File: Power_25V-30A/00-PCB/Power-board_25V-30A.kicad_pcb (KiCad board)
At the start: 2 copper layers, 14 parts, among them Q1 IRL7486, Q2 IRL7486, U1 AD8418, U2 UCC27210

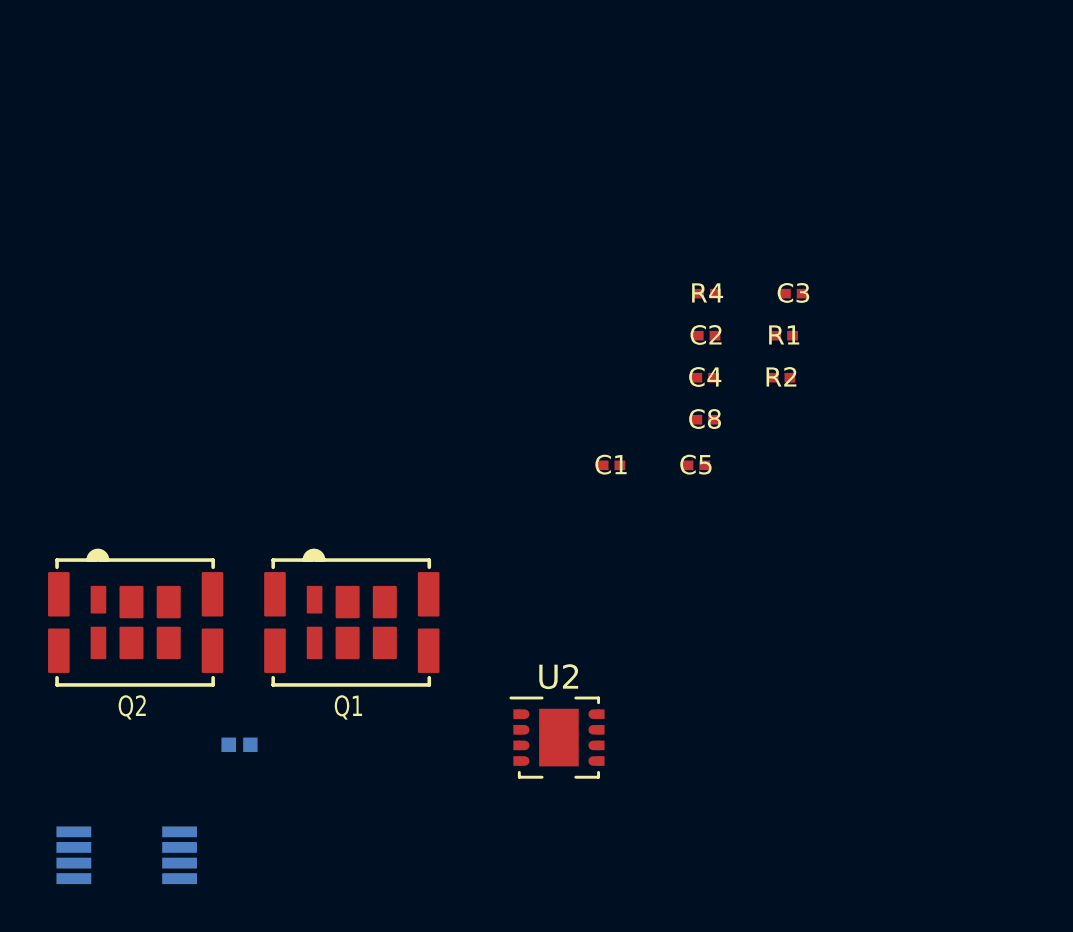
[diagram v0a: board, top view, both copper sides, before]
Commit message: Multiplied Phase Schematics
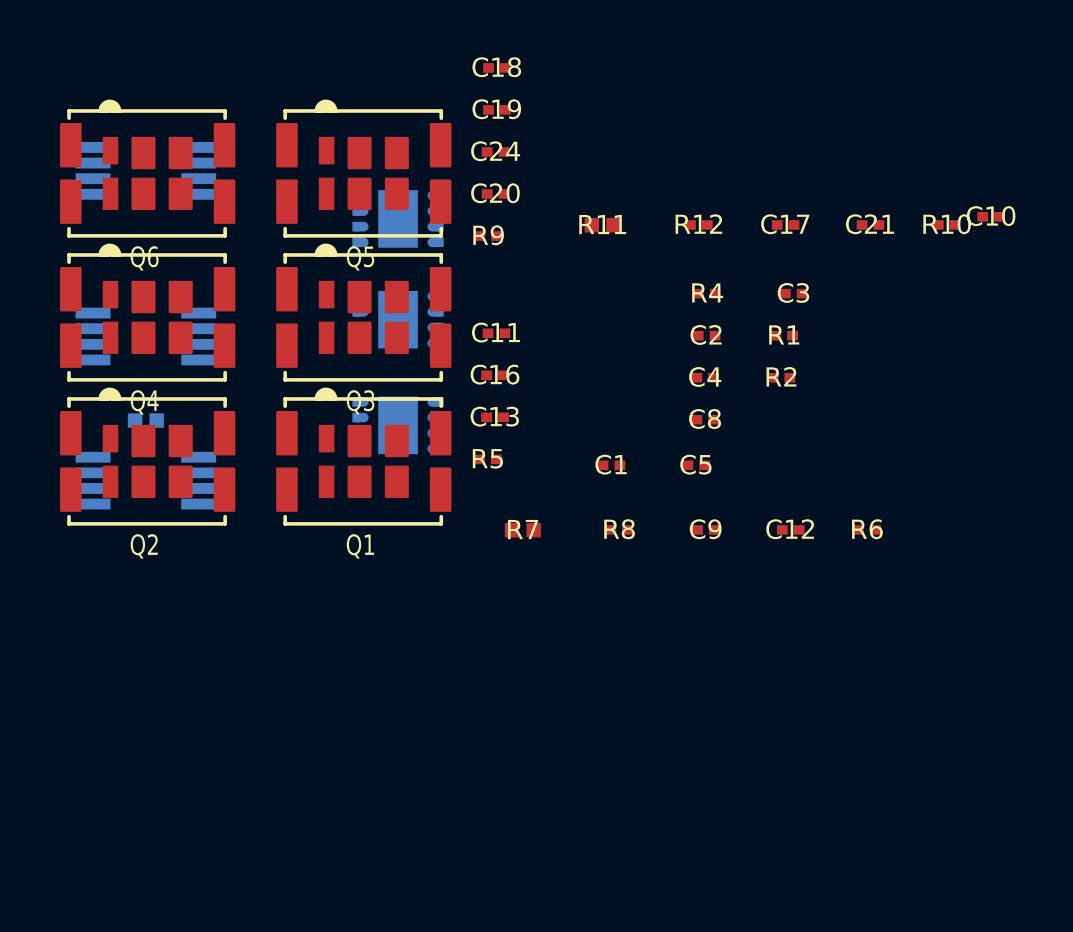
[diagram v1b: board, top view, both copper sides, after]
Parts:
- added C10: 0µF1, IPC7351-Nominal:CAPC0603X33, F.Cu at (137.2, 56.9)
- added C11: 2µF2, IPC7351-Nominal:CAPC0603X33, F.Cu at (116.6, 61.8)
- added C12: 4nF7, IPC7351-Nominal:CAPC0603X33, F.Cu at (128.9, 70.0)
- added C13: 4nF7, IPC7351-Nominal:CAPC0603X33, F.Cu at (116.5, 65.3)
- added C16: 4nF7, IPC7351-Nominal:CAPC0603X33, F.Cu at (116.5, 63.5)
- added C17: 2µF2, IPC7351-Nominal:CAPC0603X33, F.Cu at (128.6, 57.3)
- added C18: 0µF1, IPC7351-Nominal:CAPC0603X33, F.Cu at (116.6, 50.7)
- added C19: 2µF2, IPC7351-Nominal:CAPC0603X33, F.Cu at (116.6, 52.5)
- added C20: 4nF7, IPC7351-Nominal:CAPC0603X33, F.Cu at (116.6, 56.0)
- added C21: 4nF7, IPC7351-Nominal:CAPC0603X33, F.Cu at (132.2, 57.3)
- added C24: 4nF7, IPC7351-Nominal:CAPC0603X33, F.Cu at (116.6, 54.2)
- added C9: 2µF2, IPC7351-Nominal:CAPC0603X33, F.Cu at (125.3, 70.0)
- added Q3: IRL7486, Mosfet-[JS]:DirectFET-Isometric_ME, F.Cu at (110.9, 61.1)
- added Q4: IRL7486, Mosfet-[JS]:DirectFET-Isometric_ME, F.Cu at (101.9, 61.1)
- added Q5: IRL7486, Mosfet-[JS]:DirectFET-Isometric_ME, F.Cu at (110.9, 55.1)
- added Q6: IRL7486, Mosfet-[JS]:DirectFET-Isometric_ME, F.Cu at (101.9, 55.1)
- added R10: 4R7, IPC7351-Nominal:RESC0603X30, F.Cu at (135.3, 57.3)
- added R11: 0R005, IPC7351-Nominal:RESC1005X40, F.Cu at (121.0, 57.3)
- added R12: 100R, IPC7351-Nominal:RESC0603X30, F.Cu at (125.0, 57.3)
- added R5: 4R7, IPC7351-Nominal:RESC0603X30, F.Cu at (116.2, 67.0)
- added R6: 4R7, IPC7351-Nominal:RESC0603X30, F.Cu at (132.0, 70.0)
- added R7: 0R005, IPC7351-Nominal:RESC1005X40, F.Cu at (117.7, 70.0)
- added R8: 100R, IPC7351-Nominal:RESC0603X30, F.Cu at (121.7, 70.0)
- added R9: 4R7, IPC7351-Nominal:RESC0603X30, F.Cu at (116.3, 57.7)
- added U1: UCC27210, Package_SSOP:MSOP-8_3x3mm_P0.65mm, B.Cu at (102.0, 67.9)
- added U1: UCC27210, Package_SSOP:MSOP-8_3x3mm_P0.65mm, B.Cu at (102.0, 55.0)
- added U2: AD8418, Package_SON:Texas_S-PVSON-N8, B.Cu at (112.5, 65.6)
- added U2: AD8418, Package_SON:Texas_S-PVSON-N8, B.Cu at (112.5, 61.2)
- U1: value AD8418 -> UCC27210
- U2: value UCC27210 -> AD8418; moved to B.Cu
- moved U2 22.6 mm to (112.5, 57.0)
- moved U1 21.6 mm to (102.0, 61.9)
- moved R3 14.1 mm to (102.0, 65.4), turned to 0 degrees
- moved Q1 6.73 mm to (110.9, 67.1)
- moved Q2 6.73 mm to (101.9, 67.1)
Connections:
- net /Mosfet_and_current_sens/Current_Sens renamed /Phase_W/Current_Sens
- net /Mosfet_and_current_sens/Voltage_Sens_High renamed /Phase_W/Voltage_Sens_High
- C2 pad 1: Net-(C2-Pad1) -> (no net)
- R1 pad 2: Net-(R1-Pad2) -> (no net)
- R2 pad 2: Net-(R2-Pad2) -> (no net)
- U1 pad 1: Net-(R3-Pad3) -> (no net)
- U1 pad 2: GND -> (no net)
- U1 pad 3: GND -> (no net)
- U1 pad 5: Net-(R4-Pad2) -> (no net)
- U1 pad 6: VAA -> (no net)
- U1 pad 7: VAA -> (no net)
- U1 pad 8: Net-(R3-Pad2) -> (no net)
- U2 pad 1: (no net) -> Net-(R3-Pad3)
- U2 pad 2: (no net) -> GND
- U2 pad 3: (no net) -> GND
- U2 pad 4: (no net) -> Net-(U2-Pad4)
- U2 pad 5: (no net) -> Net-(R4-Pad2)
- U2 pad 6: (no net) -> VAA
- U2 pad 7: (no net) -> VAA
- U2 pad 8: (no net) -> Net-(R3-Pad2)

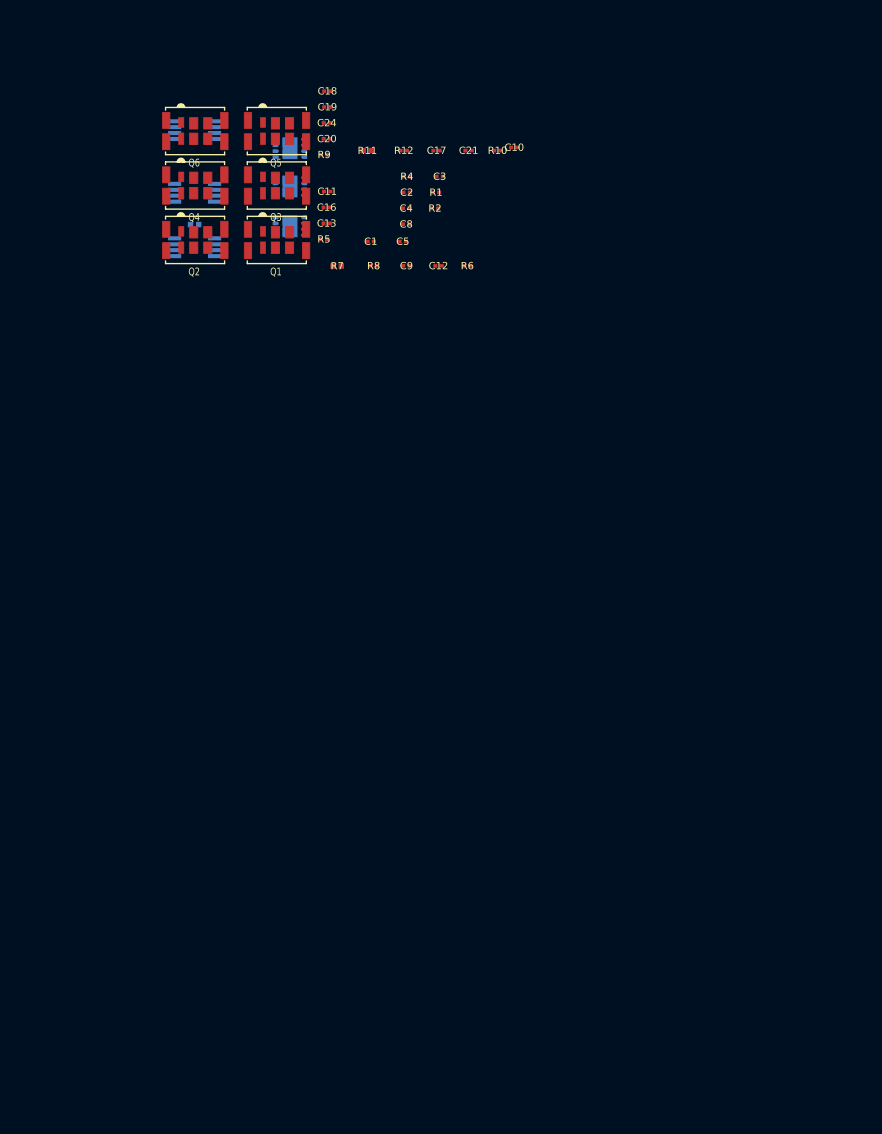
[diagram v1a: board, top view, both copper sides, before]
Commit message: Changed footprints, used new shunt footprints
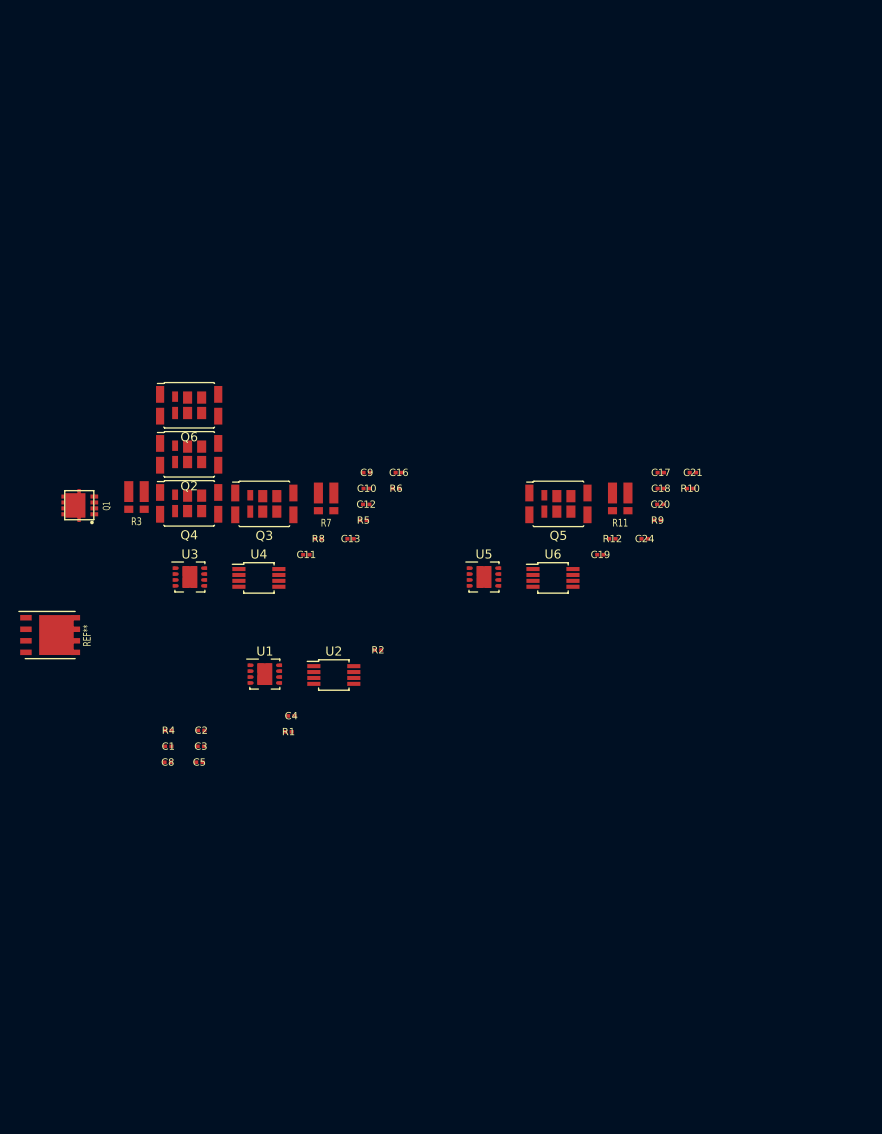
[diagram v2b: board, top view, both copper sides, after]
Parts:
- removed the U1 at (102.0, 67.9)
- removed the U1 at (102.0, 55.0)
- removed the U1 at (102.0, 61.9)
- removed the U2 at (112.5, 65.6)
- removed the U2 at (112.5, 61.2)
- removed the U2 at (112.5, 57.0)
- added REF**: SOP_Advance, Mosfet-[JS]:SOP_Advance, F.Cu at (86.1, 110.6)
- added U1: UCC27210, Package_SON:Texas_S-PVSON-N8, F.Cu at (109.7, 114.9)
- added U2: AD8418, Package_SSOP:MSOP-8_3x3mm_P0.65mm, F.Cu at (117.3, 115.0)
- added U3: UCC27210, Package_SON:Texas_S-PVSON-N8, F.Cu at (101.5, 104.2)
- added U4: AD8418, Package_SSOP:MSOP-8_3x3mm_P0.65mm, F.Cu at (109.1, 104.3)
- added U5: UCC27210, Package_SON:Texas_S-PVSON-N8, F.Cu at (133.9, 104.2)
- added U6: AD8418, Package_SSOP:MSOP-8_3x3mm_P0.65mm, F.Cu at (141.5, 104.3)
- Q1: footprint Mosfet-[JS]:DirectFET-Isometric_ME -> Mosfet-[JS]:TSON_Advance
- Q2, Q3, Q4, Q5, Q6: footprint Mosfet-[JS]:DirectFET-Isometric_ME -> Package_DirectFET:DirectFET_ME
- R11, R7: footprint IPC7351-Nominal:RESC1005X40 -> General_smd-[JS]:CSSK0612
- R3: footprint IPC7351-Nominal:RESC1005X40 -> General_smd-[JS]:CSSK0612; moved to F.Cu
- moved C3 68.0 mm to (102.7, 122.9)
- moved R4 66.4 mm to (99.1, 121.1)
- moved C8 64.8 mm to (99.0, 124.6)
- moved C2 63.4 mm to (102.7, 121.1)
- moved R1 61.6 mm to (112.3, 121.3)
- moved C5 61.6 mm to (102.5, 124.6)
- moved C1 59.9 mm to (99.1, 122.9)
- moved C19 57.7 mm to (146.7, 101.8)
- moved C24 57.6 mm to (151.6, 100.0)
- moved C4 57.3 mm to (112.6, 119.5)
- moved C18 57.1 mm to (153.3, 94.5)
- moved C20 54.5 mm to (153.3, 96.2)
- moved R9 54.5 mm to (153.0, 98.0)
- moved Q5 51.5 mm to (142.1, 96.2)
- moved R2 49.0 mm to (122.2, 112.3)
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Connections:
- C2 pad 1: (no net) -> Net-(C2-Pad1)
- R1 pad 2: (no net) -> Net-(R1-Pad2)
- R2 pad 2: (no net) -> Net-(R2-Pad2)

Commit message: testing arrangements for 3 phase power stage
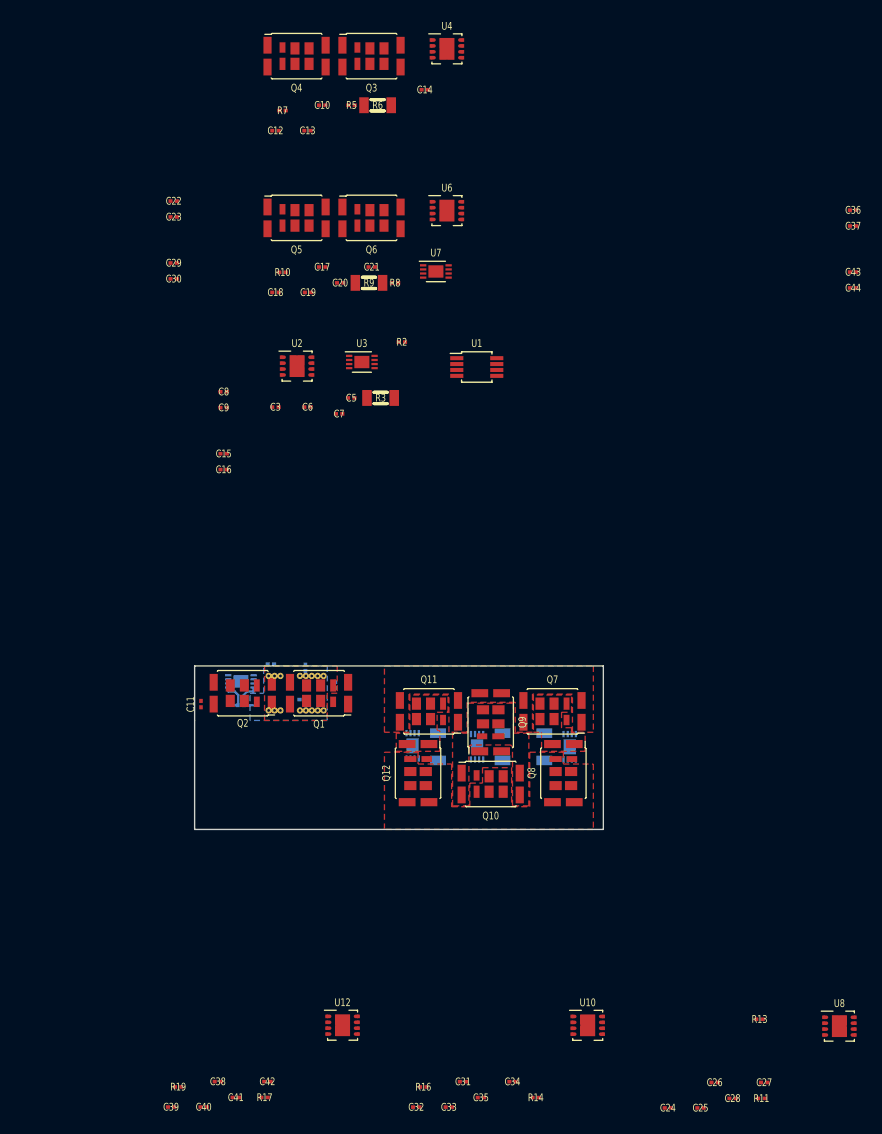
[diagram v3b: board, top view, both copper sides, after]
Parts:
- removed the REF** at (86.1, 110.6)
- added C14: 680µF_50V, IPC7351-Nominal:CAPC0603X33, F.Cu at (127.3, 50.6)
- added C15: 0µF1, IPC7351-Nominal:CAPC0603X33, F.Cu at (105.2, 90.6)
- added C22: 0µF1, IPC7351-Nominal:CAPC0603X33, F.Cu at (99.7, 62.8)
- added C23: 0µF1, IPC7351-Nominal:CAPC0603X33, F.Cu at (99.7, 64.6)
- added C25: 4nF7, IPC7351-Nominal:CAPC0603X33, F.Cu at (157.7, 162.7)
- added C26: 4nF7, IPC7351-Nominal:CAPC0603X33, F.Cu at (159.3, 159.9)
- added C27: 680µF_50V, IPC7351-Nominal:CAPC0603X33, F.Cu at (164.7, 159.9)
- added C28: 680µF_50V, IPC7351-Nominal:CAPC0603X33, F.Cu at (161.2, 161.6)
- added C29: 0µF1, IPC7351-Nominal:CAPC0603X33, F.Cu at (99.7, 69.6)
- added C30: 0µF1, IPC7351-Nominal:CAPC0603X33, F.Cu at (99.7, 71.4)
- added C31: 2µF2, IPC7351-Nominal:CAPC0603X33, F.Cu at (131.5, 159.8)
- added C32: 4nF7, IPC7351-Nominal:CAPC0603X33, F.Cu at (126.4, 162.6)
- added C33: 4nF7, IPC7351-Nominal:CAPC0603X33, F.Cu at (130.0, 162.6)
- added C34: 680µF_50V, IPC7351-Nominal:CAPC0603X33, F.Cu at (137.0, 159.8)
- added C35: 680µF_50V, IPC7351-Nominal:CAPC0603X33, F.Cu at (133.5, 161.5)
- added C36: 0µF1, IPC7351-Nominal:CAPC0603X33, F.Cu at (174.5, 63.8)
- added C37: 0µF1, IPC7351-Nominal:CAPC0603X33, F.Cu at (174.5, 65.6)
- added C38: 2µF2, IPC7351-Nominal:CAPC0603X33, F.Cu at (104.6, 159.8)
- added C39: 4nF7, IPC7351-Nominal:CAPC0603X33, F.Cu at (99.4, 162.6)
- added C40: 4nF7, IPC7351-Nominal:CAPC0603X33, F.Cu at (103.0, 162.6)
- added C41: 680µF_50V, IPC7351-Nominal:CAPC0603X33, F.Cu at (106.5, 161.5)
- added C42: 680µF_50V, IPC7351-Nominal:CAPC0603X33, F.Cu at (110.0, 159.8)
- added C43: 0µF1, IPC7351-Nominal:CAPC0603X33, F.Cu at (174.5, 70.6)
- added C44: 0µF1, IPC7351-Nominal:CAPC0603X33, F.Cu at (174.5, 72.4)
- added C6: 680µF_50V, IPC7351-Nominal:CAPC0603X33, F.Cu at (114.4, 85.5)
- added C7: 680µF_50V, IPC7351-Nominal:CAPC0603X33, F.Cu at (117.9, 86.2)
- added Q10: IRL7486, Mosfet-[JS]:DirectFET_ME, F.Cu at (134.6, 127.0)
- added Q11: IRL7486, Mosfet-[JS]:DirectFET_ME, F.Cu at (127.8, 119.0)
- added Q12: IRL7486, Mosfet-[JS]:DirectFET_ME, F.Cu at (126.6, 125.8)
- added Q7: IRL7486, Mosfet-[JS]:DirectFET_ME, F.Cu at (141.4, 119.0)
- added Q8: IRL7486, Mosfet-[JS]:DirectFET_ME, F.Cu at (142.6, 125.8)
- added Q9: IRL7486, Mosfet-[JS]:DirectFET_ME, F.Cu at (134.6, 120.2)
- added R13: 4R7, IPC7351-Nominal:RESC0603X30, F.Cu at (164.2, 152.9)
- added R14: 4R7, IPC7351-Nominal:RESC0603X30, F.Cu at (139.6, 161.5)
- added R15: 0R0005, IPC7351-Nominal:RESC3216X63, B.Cu at (135.9, 122.9)
- added R16: 4R7, IPC7351-Nominal:RESC0603X30, F.Cu at (127.2, 160.4)
- added R17: 4R7, IPC7351-Nominal:RESC0603X30, F.Cu at (109.7, 161.5)
- added R18: 0R0005, IPC7351-Nominal:RESC3216X63, B.Cu at (128.8, 122.9)
- added R19: 4R7, IPC7351-Nominal:RESC0603X30, F.Cu at (100.2, 160.4)
- added REF**: Stitching_Via-0_7mm, stitching_vias:Stitching_Via-0_7mm, F.Cu at (110.2, 115.1)
- added REF**: Stitching_Via-0_7mm, stitching_vias:Stitching_Via-0_7mm, F.Cu at (110.8, 118.9)
- added REF**: Stitching_Via-0_7mm, stitching_vias:Stitching_Via-0_7mm, F.Cu at (111.5, 118.9)
- added REF**: Stitching_Via-0_7mm, stitching_vias:Stitching_Via-0_7mm, F.Cu at (113.6, 118.9)
- added REF**: Stitching_Via-0_7mm, stitching_vias:Stitching_Via-0_7mm, F.Cu at (114.2, 118.9)
- added REF**: Stitching_Via-0_7mm, stitching_vias:Stitching_Via-0_7mm, F.Cu at (114.9, 118.9)
- added REF**: Stitching_Via-0_7mm, stitching_vias:Stitching_Via-0_7mm, F.Cu at (115.5, 118.9)
- added REF**: Stitching_Via-0_7mm, stitching_vias:Stitching_Via-0_7mm, F.Cu at (116.2, 118.9)
- added REF**: Stitching_Via-0_7mm, stitching_vias:Stitching_Via-0_7mm, F.Cu at (110.8, 115.1)
- added REF**: Stitching_Via-0_7mm, stitching_vias:Stitching_Via-0_7mm, F.Cu at (115.5, 115.1)
- added REF**: Stitching_Via-0_7mm, stitching_vias:Stitching_Via-0_7mm, F.Cu at (111.5, 115.1)
- added REF**: Stitching_Via-0_7mm, stitching_vias:Stitching_Via-0_7mm, F.Cu at (113.6, 115.1)
- added REF**: Stitching_Via-0_7mm, stitching_vias:Stitching_Via-0_7mm, F.Cu at (114.9, 115.1)
- added REF**: Stitching_Via-0_7mm, stitching_vias:Stitching_Via-0_7mm, F.Cu at (114.2, 115.1)
- added REF**: Stitching_Via-0_7mm, stitching_vias:Stitching_Via-0_7mm, F.Cu at (116.2, 115.1)
- added REF**: Stitching_Via-0_7mm, stitching_vias:Stitching_Via-0_7mm, F.Cu at (110.2, 118.9)
- added U10: UCC27210, Package_SON:Texas_S-PVSON-N8, F.Cu at (145.3, 153.6)
- added U11: LT6118, Package_DFN_QFN:DFN-8-1EP_3x2mm_P0.45mm, B.Cu at (133.1, 122.9)
- added U12: UCC27210, Package_SON:Texas_S-PVSON-N8, F.Cu at (118.3, 153.6)
- added U13: LT6118, Package_DFN_QFN:DFN-8-1EP_3x2mm_P0.45mm, B.Cu at (126.0, 122.8)
- added U7: LT6118, Package_DFN_QFN:DFN-8-1EP_3x2mm_P0.45mm, F.Cu at (128.6, 70.6)
- added U8: UCC27210, Package_SON:Texas_S-PVSON-N8, F.Cu at (173.0, 153.7)
- added U9: LT6118, Package_DFN_QFN:DFN-8-1EP_3x2mm_P0.45mm, B.Cu at (143.3, 122.9)
- C1: value 2µF2 -> 4nF7; moved to B.Cu
- C10: value 0µF1 -> 2µF2
- C11, C19: value 2µF2 -> 4nF7
- C13, C20, C21: value 4nF7 -> 680µF_50V
- C16, C8: value 4nF7 -> 0µF1
- C18: value 0µF1 -> 4nF7
- C2: value 0µF1 -> 2µF2; moved to B.Cu
- C24: value 4nF7 -> 2µF2
- C4: moved to B.Cu
- C9: value 2µF2 -> 0µF1
- Q1: footprint Mosfet-[JS]:TSON_Advance -> Mosfet-[JS]:DirectFET_ME
- Q2, Q3, Q4, Q5, Q6: footprint Package_DirectFET:DirectFET_ME -> Mosfet-[JS]:DirectFET_ME
- R1: value 4R7 -> 100R; moved to B.Cu
- R11, R7: value 0R005 -> 4R7; footprint General_smd-[JS]:CSSK0612 -> IPC7351-Nominal:RESC0603X30
- R12: value 100R -> 0R0005; footprint IPC7351-Nominal:RESC0603X30 -> IPC7351-Nominal:RESC3216X63; moved to B.Cu
- R3: value 0R005 -> 0R0005; footprint General_smd-[JS]:CSSK0612 -> IPC7351-Nominal:RESC3216X63
- R4: value 100R -> 4R7; moved to B.Cu
- R6, R9: value 4R7 -> 0R0005; footprint IPC7351-Nominal:RESC0603X30 -> IPC7351-Nominal:RESC3216X63
- R8: value 100R -> 4R7
- U1: value UCC27210 -> AD8418; footprint Package_SON:Texas_S-PVSON-N8 -> Package_SSOP:MSOP-8_3x3mm_P0.65mm
- U2, U4, U6: value AD8418 -> UCC27210; footprint Package_SSOP:MSOP-8_3x3mm_P0.65mm -> Package_SON:Texas_S-PVSON-N8
- U3: value UCC27210 -> LT6118; footprint Package_SON:Texas_S-PVSON-N8 -> Package_DFN_QFN:DFN-8-1EP_3x2mm_P0.45mm
- U5: value UCC27210 -> LT6118; footprint Package_SON:Texas_S-PVSON-N8 -> Package_DFN_QFN:DFN-8-1EP_3x2mm_P0.45mm; moved to B.Cu
- moved R11 67.9 mm to (164.4, 161.6)
- moved C24 62.7 mm to (154.1, 162.7)
- moved U4 61.8 mm to (129.8, 46.1)
- moved R10 50.8 mm to (111.7, 70.7)
- moved Q3 50.7 mm to (121.5, 46.9)
- moved Q4 50.6 mm to (113.2, 46.9)
- moved C18 47.6 mm to (110.9, 72.9)
- moved R5 45.7 mm to (119.3, 52.3)
- moved C13 45.2 mm to (114.4, 55.1)
- moved C17 43.6 mm to (116.0, 70.1)
- moved C5 43.5 mm to (119.2, 84.5)
- moved C19 43.2 mm to (114.5, 72.9)
- moved R7 43.0 mm to (111.7, 52.9)
- moved C20 42.9 mm to (118.0, 71.8)
- moved Q5 42.7 mm to (113.2, 64.7)
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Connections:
- net /sheet5A1C1425/PWM_Low_Fet renamed /Phase_U/Current_Sens
- net /sheet5A1C15A8/PWM_Low_Fet renamed /Phase_V/Current_Sens
- C1 pad 1: VAA -> Net-(C1-Pad1)
- C10 pad 1: Net-(C10-Pad1) -> VCC
- C10 pad 2: /sheet5A1C1425/Voltage_Sens_High -> GND
- C11 pad 1: VAA -> +VDC
- C16 pad 1: /sheet5A1C1425/Current_Sens -> VCC
- C17 pad 1: VAA -> VCC
- C18 pad 1: Net-(C18-Pad1) -> +VDC
- C18 pad 2: /sheet5A1C15A8/Voltage_Sens_High -> GND
- C19 pad 1: VAA -> +VDC
- C2 pad 1: Net-(C2-Pad1) -> VAA
- C2 pad 2: /Phase_W/Voltage_Sens_High -> GND
- C24 pad 1: /sheet5A1C15A8/Current_Sens -> VCC
- C3 pad 1: VAA -> VCC
- C8 pad 1: /Phase_W/Current_Sens -> Net-(C8-Pad1)
- C8 pad 2: GND -> /Phase_U/Voltage_Sens_High
- C9 pad 1: VAA -> VCC
- Q1 pad 1: Net-(Q1-Pad1) -> +VDC
- Q1 pad 2: /Phase_W/Voltage_Sens_High -> Net-(Q1-Pad2)
- Q1 pad 3: +VDC -> /Phase_U/Voltage_Sens_High
- Q2 pad 1: Net-(Q2-Pad1) -> /Phase_U/Voltage_Sens_High
- Q2 pad 2: GND -> Net-(Q2-Pad2)
- Q2 pad 3: /Phase_W/Voltage_Sens_High -> GND
- Q3 pad 1: Net-(Q3-Pad1) -> +VDC
- Q3 pad 2: /sheet5A1C1425/Voltage_Sens_High -> Net-(Q3-Pad2)
- Q3 pad 3: +VDC -> /Phase_V/Voltage_Sens_High
- Q4 pad 1: Net-(Q4-Pad1) -> /Phase_V/Voltage_Sens_High
- Q4 pad 2: GND -> Net-(Q4-Pad2)
- Q4 pad 3: /sheet5A1C1425/Voltage_Sens_High -> GND
- Q5 pad 1: Net-(Q5-Pad1) -> +VDC
- Q5 pad 2: /sheet5A1C15A8/Voltage_Sens_High -> Net-(Q5-Pad2)
- Q5 pad 3: +VDC -> /Phase_W/Voltage_Sens_High
- Q6 pad 1: Net-(Q6-Pad1) -> /Phase_W/Voltage_Sens_High
- Q6 pad 2: GND -> Net-(Q6-Pad2)
- Q6 pad 3: /sheet5A1C15A8/Voltage_Sens_High -> GND
- R1 pad 1: Net-(Q1-Pad1) -> Net-(C1-Pad1)
- R10 pad 1: Net-(Q6-Pad1) -> Net-(Q6-Pad2)
- R11 pad 1: /sheet5A1C15A8/Voltage_Sens_High -> Net-(Q7-Pad2)
- R12 pad 1: /sheet5A1C15A8/Current_Sens -> /Phase_X/Phase_Current_Out
- R12 pad 2: Net-(R12-Pad2) -> /Phase_X/Voltage_Sens_High
- R2 pad 1: Net-(Q2-Pad1) -> Net-(Q1-Pad2)
- R3 pad 1: /Phase_W/Voltage_Sens_High -> /Phase_U/Phase_Current_Out
- R3 pad 2: Net-(R3-Pad2) -> /Phase_U/Voltage_Sens_High
- R4 pad 1: /Phase_W/Current_Sens -> Net-(Q2-Pad2)
- R5 pad 1: Net-(Q3-Pad1) -> Net-(Q3-Pad2)
- R6 pad 1: Net-(Q4-Pad1) -> /Phase_V/Phase_Current_Out
- R6 pad 2: Net-(R6-Pad2) -> /Phase_V/Voltage_Sens_High
- R7 pad 1: /sheet5A1C1425/Voltage_Sens_High -> Net-(Q4-Pad2)
- R8 pad 1: /sheet5A1C1425/Current_Sens -> Net-(Q5-Pad2)
- R9 pad 1: Net-(Q5-Pad1) -> /Phase_W/Phase_Current_Out
- R9 pad 2: Net-(R9-Pad2) -> /Phase_W/Voltage_Sens_High
- U1 pad 1: VAA -> (no net)
- U1 pad 2: Net-(C2-Pad1) -> GND
- U1 pad 3: Net-(R1-Pad2) -> GND
- U1 pad 4: /Phase_W/Voltage_Sens_High -> (no net)
- U1 pad 5: /Phase_W/PWM_High_Fet -> Net-(R1-Pad2)
- U1 pad 6: /Phase_W/PWM_Low_Fet -> VAA
- U1 pad 7: GND -> VAA
- U1 pad 8: Net-(R2-Pad2) -> (no net)
- U2 pad 1: Net-(R3-Pad3) -> VCC
- U2 pad 2: GND -> Net-(C8-Pad1)
- U2 pad 3: GND -> Net-(R2-Pad2)
- U2 pad 4: Net-(U2-Pad4) -> /Phase_U/Voltage_Sens_High
- U2 pad 5: Net-(R4-Pad2) -> /Phase_U/PWM_High_Fet
- U2 pad 6: VAA -> /Phase_U/PWM_Low_Fet
- U2 pad 7: VAA -> GND
- U2 pad 8: Net-(R3-Pad2) -> Net-(R4-Pad2)
- U3 pad 1: VAA -> /Phase_U/Phase_Current_Out
- U3 pad 2: Net-(C10-Pad1) -> GND
- U3 pad 3: Net-(R5-Pad2) -> (no net)
- U3 pad 4: /sheet5A1C1425/Voltage_Sens_High -> GND
- U3 pad 5: /sheet5A1C1425/PWM_High_Fet -> GND
- U3 pad 7: GND -> VCC
- U3 pad 8: Net-(R6-Pad2) -> /Phase_U/Voltage_Sens_High
- U4 pad 1: Net-(R7-Pad3) -> VCC
- U4 pad 2: GND -> Net-(C15-Pad1)
- U4 pad 3: GND -> Net-(R5-Pad2)
- U4 pad 4: Net-(U4-Pad4) -> /Phase_V/Voltage_Sens_High
- U4 pad 5: Net-(R8-Pad2) -> /Phase_V/PWM_High_Fet
- U4 pad 6: VAA -> /Phase_V/PWM_Low_Fet
- U4 pad 7: VAA -> GND
- U5 pad 1: VAA -> /Phase_V/Phase_Current_Out
- U5 pad 2: Net-(C18-Pad1) -> GND
- U5 pad 3: Net-(R9-Pad2) -> Net-(U5-Pad3)
- U5 pad 4: /sheet5A1C15A8/Voltage_Sens_High -> GND
- U5 pad 5: /sheet5A1C15A8/PWM_High_Fet -> GND
- U5 pad 7: GND -> VCC
- U5 pad 8: Net-(R10-Pad2) -> /Phase_V/Voltage_Sens_High
- U6 pad 1: Net-(R11-Pad3) -> VCC
- U6 pad 2: GND -> Net-(C22-Pad1)
- U6 pad 3: GND -> Net-(R8-Pad2)
- U6 pad 4: Net-(U6-Pad4) -> /Phase_W/Voltage_Sens_High
- U6 pad 5: Net-(R12-Pad2) -> /Phase_W/PWM_High_Fet
- U6 pad 6: VAA -> /Phase_W/PWM_Low_Fet
- U6 pad 7: VAA -> GND
- U6 pad 8: Net-(R11-Pad2) -> Net-(R10-Pad2)
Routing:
- net /Phase_W/Phase_Current_Out: track 0.00 -> 3.90 mm
- net /Phase_W/Voltage_Sens_High: track 0.00 -> 3.90 mm
- added copper zone on F.Cu, net +VDC
- added copper zone on B.Cu, net /Phase_W/Voltage_Sens_High
- added copper zone on F.Cu, net /Phase_W/Voltage_Sens_High
- added copper zone on F.Cu, net /Phase_X/Voltage_Sens_High
- added copper zone on F.Cu, net /Phase_Y/Voltage_Sens_High
- added copper zone on F.Cu, net /Phase_Z/Voltage_Sens_High
- added copper zone on F.Cu, net GND
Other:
- board outline added: 45 x 18 mm
